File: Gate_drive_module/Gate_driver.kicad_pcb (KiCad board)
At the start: 2 copper layers, 34 parts, among them J1 CONN_01X10, J2 CONN_01X04, J3 CONN_01X03, J4 CONN_01X03, J5 CONN_01X03, U1 HCPL-316J, U2 Mornsun_QA01C

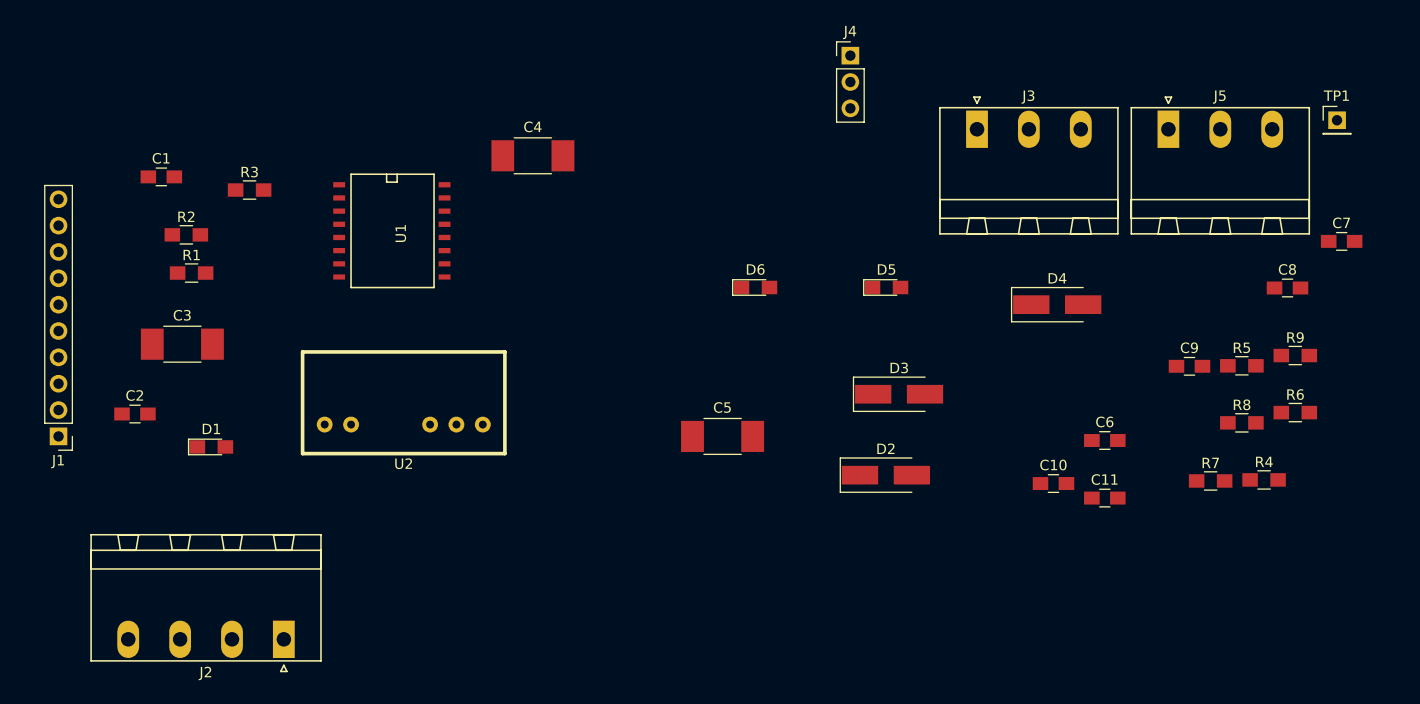
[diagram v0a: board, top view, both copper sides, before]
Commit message: Fixed 3d shape configuration for cross platform dev. (I hope)
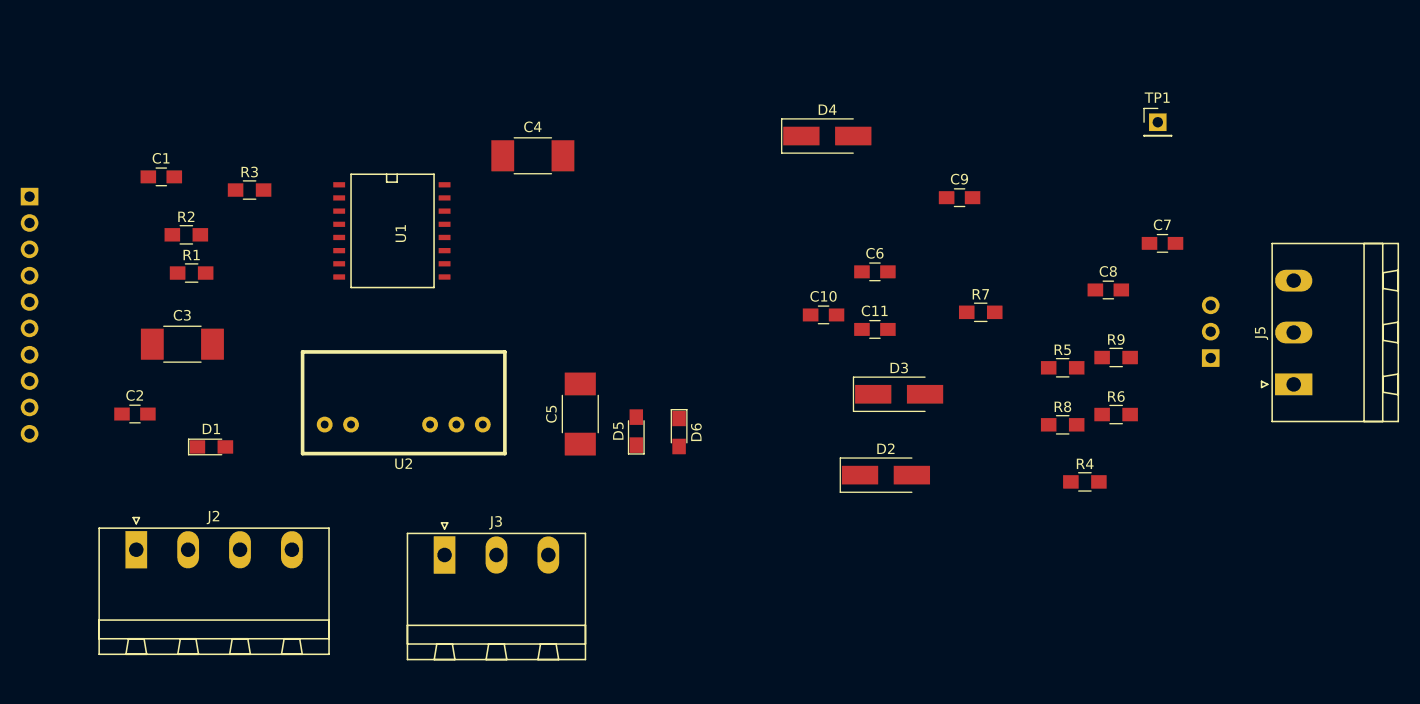
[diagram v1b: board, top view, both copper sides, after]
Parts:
- J1, J4: moved to B.Cu
- moved J3 65.7 mm to (140.5, 152.0)
- moved J4 45.3 mm to (214.3, 133.0)
- moved D5 27.8 mm to (158.9, 140.1), turned to 90 degrees
- moved R7 27.5 mm to (192.1, 128.6)
- moved C10 27.5 mm to (177.0, 128.9)
- moved C11 27.5 mm to (181.9, 130.3)
- moved C6 27.5 mm to (181.9, 124.7)
- moved C9 27.5 mm to (190.1, 117.6)
- moved D4 27.5 mm to (177.4, 111.6)
- moved J5 27.4 mm to (222.3, 135.6), turned to 90 degrees
- moved J1 23.3 mm to (100.5, 117.5)
- moved C8 17.3 mm to (204.4, 126.5)
- moved R6 17.3 mm to (205.2, 138.5)
- moved R9 17.3 mm to (205.2, 133.0)
- moved C7 17.3 mm to (209.7, 122.0)
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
